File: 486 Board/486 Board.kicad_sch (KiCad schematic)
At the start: 35 parts

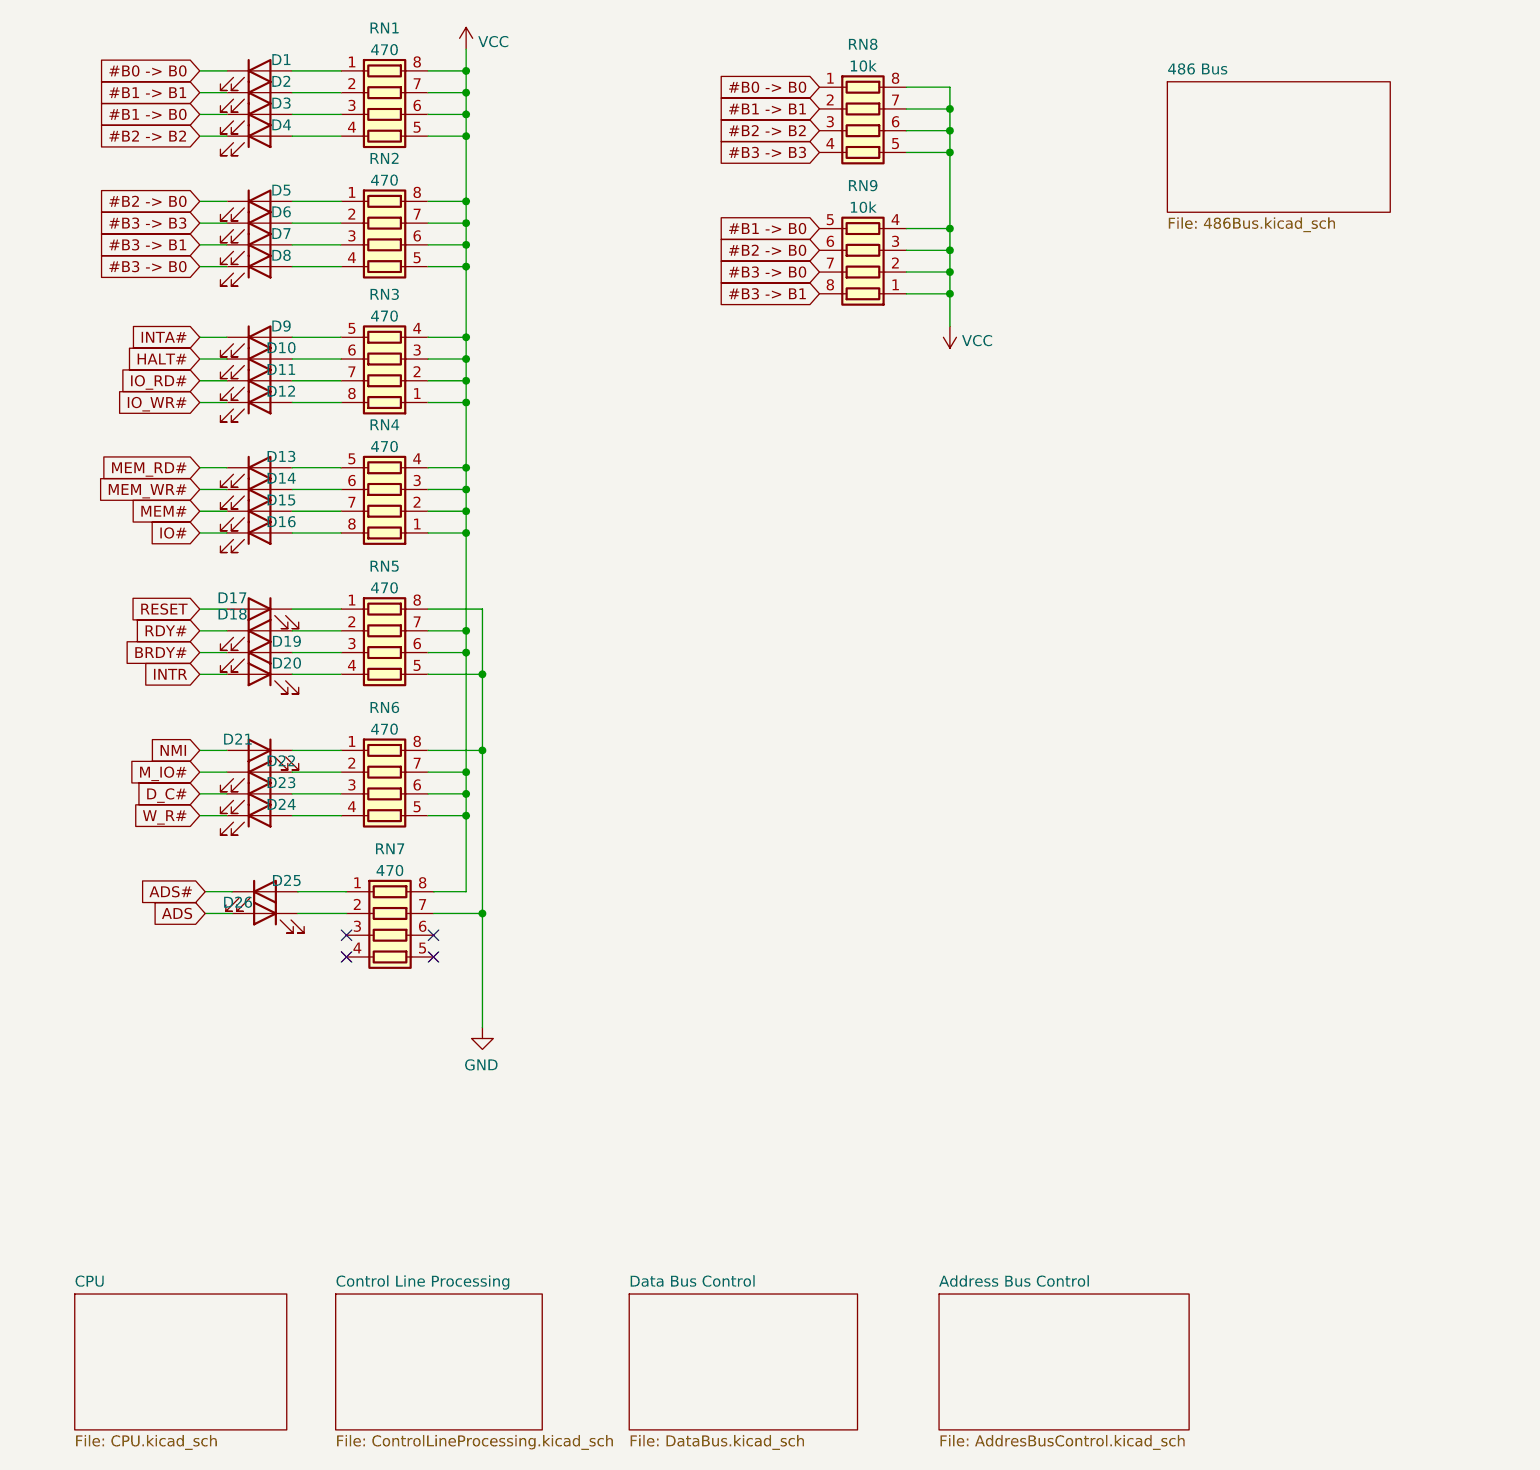
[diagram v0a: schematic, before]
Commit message: * Layout Template for eurocard format * 486 Board updated to new layout * Support board draft * Added 6u eurocard backplane meant for ATX case
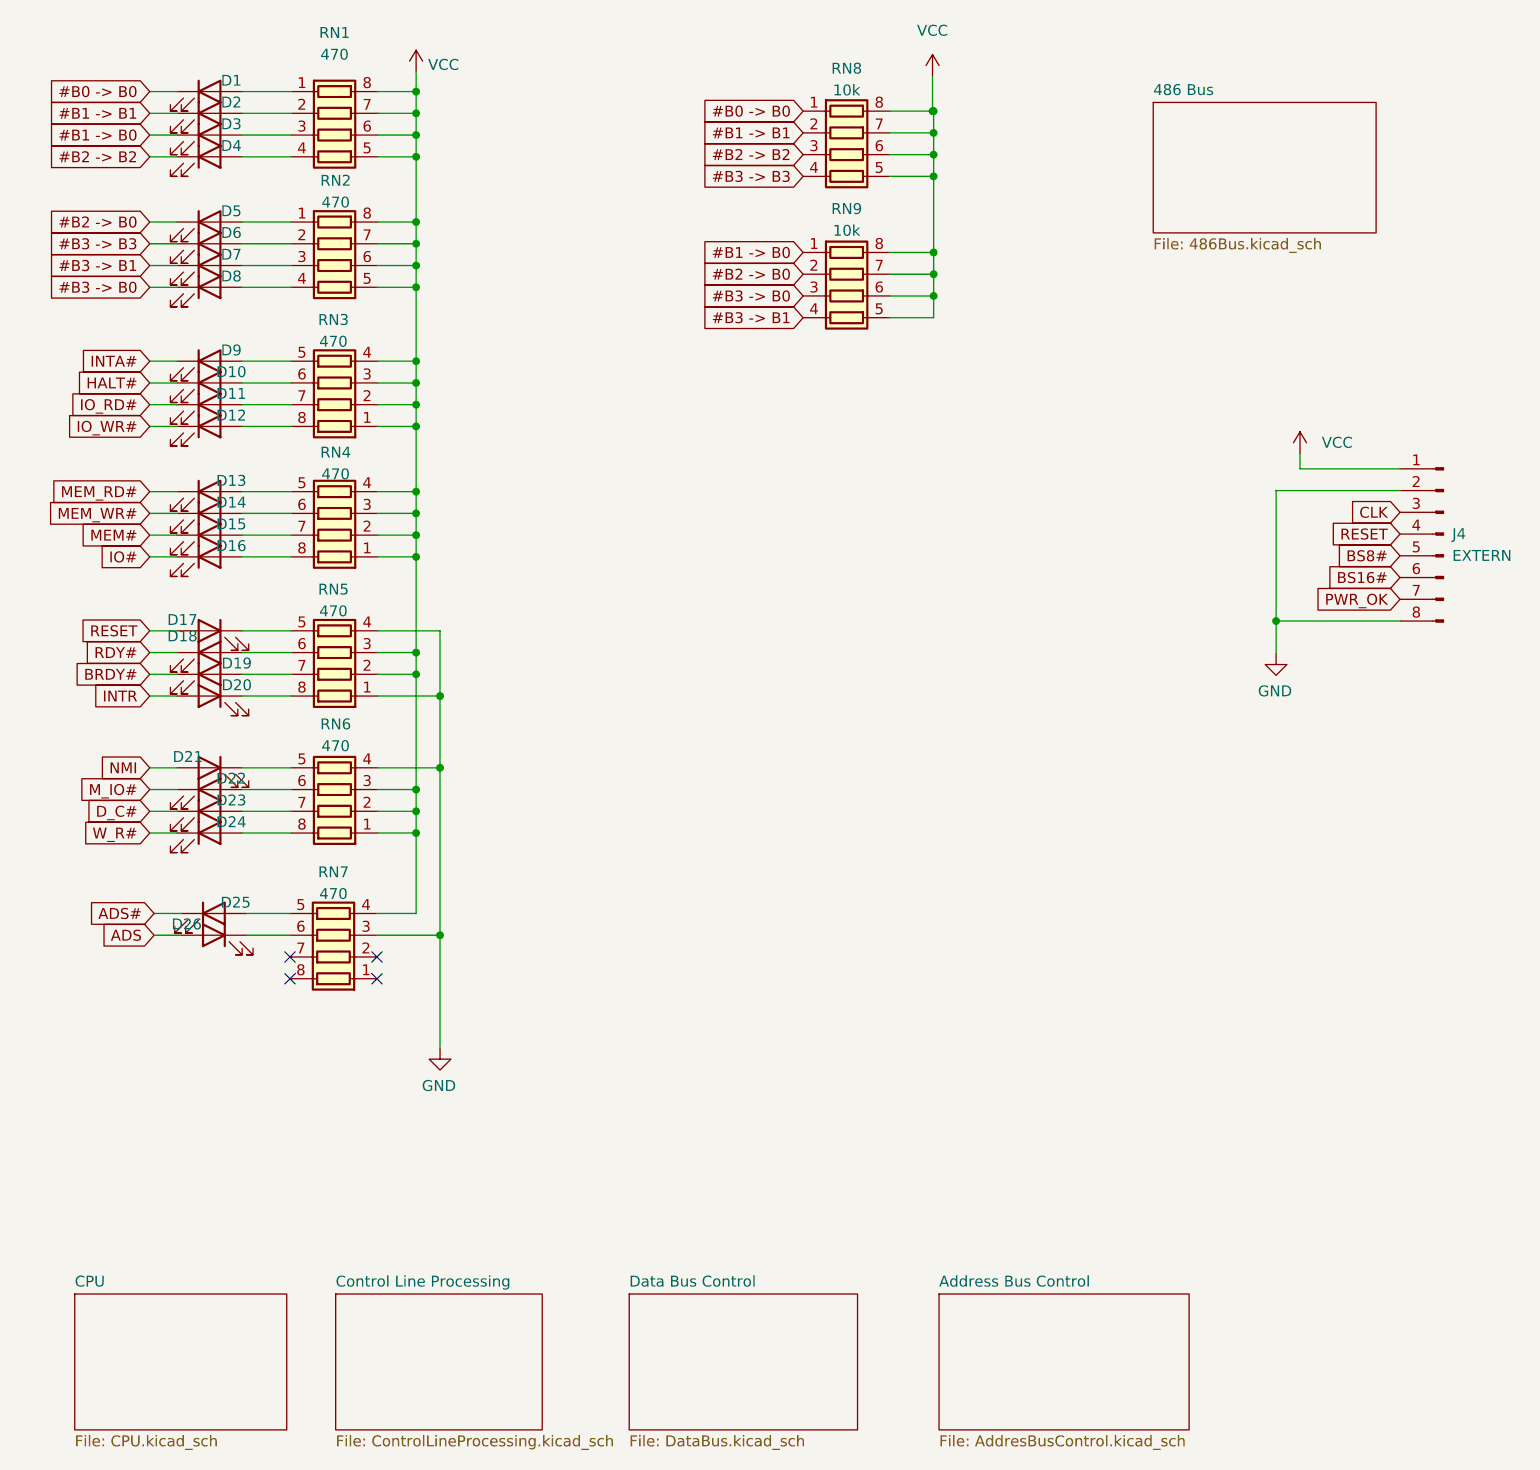
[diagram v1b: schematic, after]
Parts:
- added J4: EXTERN, Connector_PinSocket_2.54mm:PinSocket_1x08_P2.54mm_Vertical, symbol Connector:Conn_01x08_Male
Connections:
- net #B1 -> B0: now also RN9.1 (R1.1); no longer RN9.5 (R4.2)
- net #B2 -> B0: now also RN9.2 (R2.1); no longer RN9.6 (R3.2)
- net #B3 -> B0: now also RN9.3 (R3.1); no longer RN9.7 (R2.2)
- net #B3 -> B1: now also RN9.4 (R4.1); no longer RN9.8 (R1.2)
- net GND: now also RN5.1 (R1.1), RN5.4 (R4.1), RN6.4 (R4.1), RN7.3 (R3.1), J4.2 (Pin_2), J4.8 (Pin_8); no longer RN5.5 (R4.2), RN5.8 (R1.2), RN6.8 (R1.2), RN7.7 (R2.2)
- net RESET: now also J4.4 (Pin_4)
- net VCC: now also RN5.2 (R2.1), RN5.3 (R3.1), RN6.1 (R1.1), RN6.2 (R2.1), RN6.3 (R3.1), RN7.4 (R4.1), RN9.5 (R4.2), RN9.6 (R3.2), RN9.7 (R2.2), RN9.8 (R1.2), J4.1 (Pin_1); no longer RN5.6 (R3.2), RN5.7 (R2.2), RN6.5 (R4.2), RN6.6 (R3.2), RN6.7 (R2.2), RN7.8 (R1.2), RN9.1 (R1.1), RN9.2 (R2.1), RN9.3 (R3.1), RN9.4 (R4.1)
- net at D24.2 (A): now also RN6.8 (R1.2); no longer RN6.4 (R4.1)
- net at D21.1 (K): now also RN6.5 (R4.2); no longer RN6.1 (R1.1)
- net at D22.2 (A): now also RN6.6 (R3.2); no longer RN6.2 (R2.1)
- net at D19.2 (A): now also RN5.7 (R2.2); no longer RN5.3 (R3.1)
- net at D18.2 (A): now also RN5.6 (R3.2); no longer RN5.2 (R2.1)
- net at D23.2 (A): now also RN6.7 (R2.2); no longer RN6.3 (R3.1)
- net at D26.1 (K): now also RN7.6 (R3.2); no longer RN7.2 (R2.1)
- net at D17.1 (K): now also RN5.5 (R4.2); no longer RN5.1 (R1.1)
- net at D20.1 (K): now also RN5.8 (R1.2); no longer RN5.4 (R4.1)
- net at RN7.1 (R1.1): no longer D25.2 (A)
- net at RN7.5 (R4.2): now also D25.2 (A)
- new net BS16#: J4.6 (Pin_6)
- new net BS8#: J4.5 (Pin_5)
- new net CLK: J4.3 (Pin_3)
- new net PWR_OK: J4.7 (Pin_7)
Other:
- moved on the sheet: D1, D10, D11, D12, D13, D14, D15, D16, D17, D18, D19, D2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
